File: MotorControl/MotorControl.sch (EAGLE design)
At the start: 6 parts

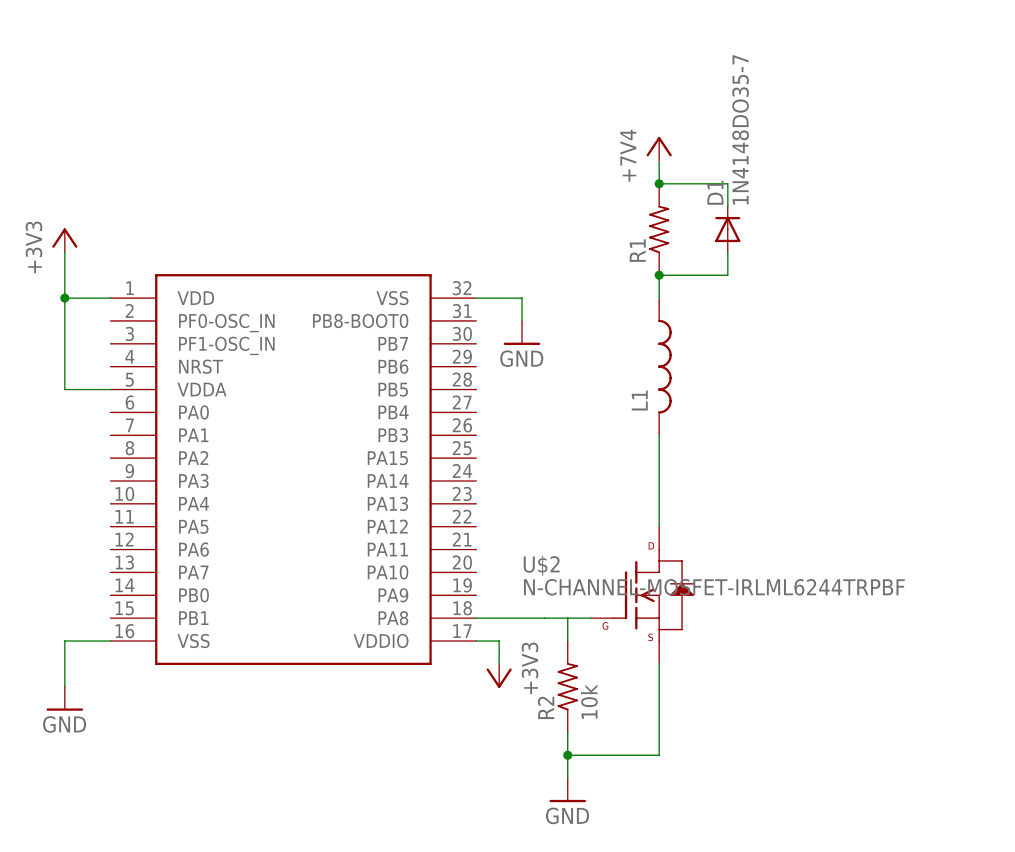
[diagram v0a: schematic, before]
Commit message: Update motor control schematic
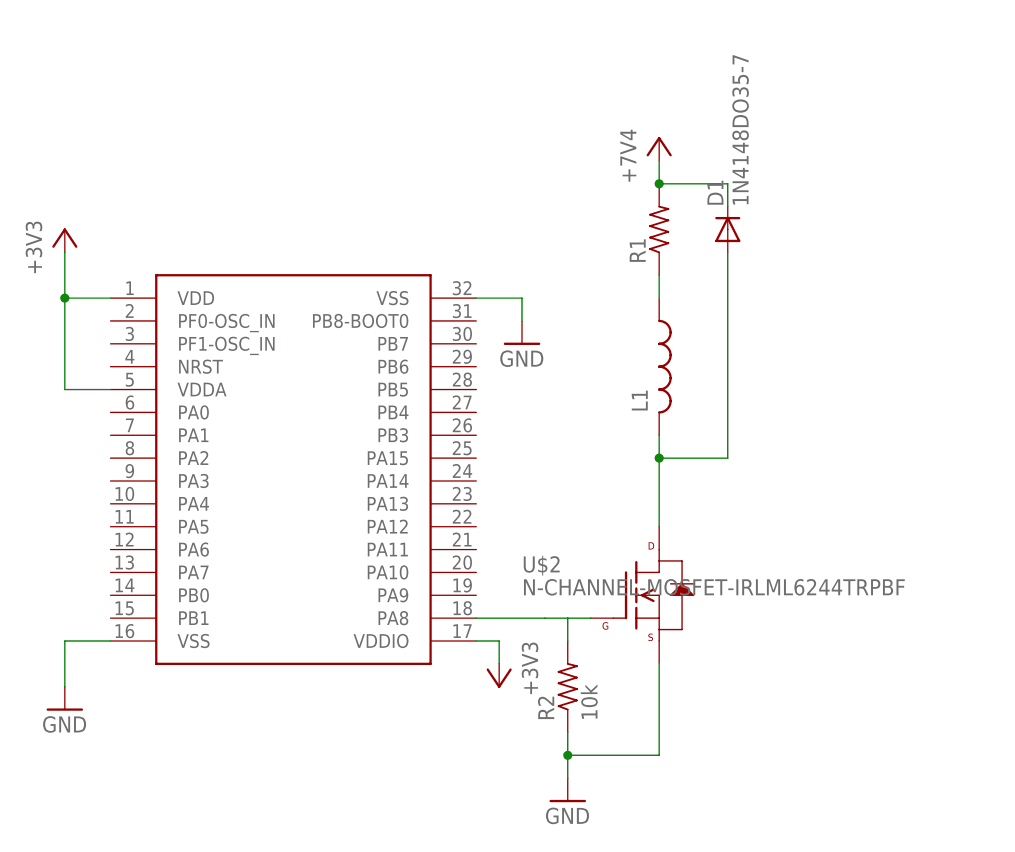
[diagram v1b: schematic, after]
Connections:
- removed net N$4: L1.2, U$2.D
- new net N$2: L1.1, R1.1
- net N$5: now also L1.2, U$2.D; no longer L1.1, R1.1
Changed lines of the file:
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@@
-</segment>
-</net>
-<net name="N$4" class="0">
-<segment>
-<pinref part="U$2" gate="G$1" pin="D"/>
-<pinref part="L1" gate="G$1" pin="2"/>
-<wire x1="40.64" y1="-2.54" x2="40.64" y2="7.62" width="0.1524" layer="91"/>
 </segment>
 </net>
 <net name="N$5" class="0">
 <segment>
-<pinref part="L1" gate="G$1" pin="1"/>
-<pinref part="R1" gate="G$1" pin="1"/>
-<wire x1="40.64" y1="22.86" x2="40.64" y2="25.4" width="0.1524" layer="91"/>
 <pinref part="D1" gate="G$1" pin="A"/>
-<wire x1="40.64" y1="25.4" x2="48.26" y2="25.4" width="0.1524" layer="91"/>
-<wire x1="48.26" y1="25.4" x2="48.26" y2="27.94" width="0.1524" layer="91"/>
-<junction x="40.64" y="25.4"/>
+<pinref part="U$2" gate="G$1" pin="D"/>
+<pinref part="L1" gate="G$1" pin="2"/>
+<wire x1="40.64" y1="-2.54" x2="40.64" y2="5.08" width="0.1524" layer="91"/>
+<wire x1="40.64" y1="5.08" x2="40.64" y2="7.62" width="0.1524" layer="91"/>
+<wire x1="48.26" y1="27.94" x2="48.26" y2="5.08" width="0.1524" layer="91"/>
+<wire x1="48.26" y1="5.08" x2="40.64" y2="5.08" width="0.1524" layer="91"/>
+<junction x="40.64" y="5.08"/>
 </segment>
 </net>
@@
 </segment>
 </net>
+<net name="N$2" class="0">
+<segment>
+<pinref part="R1" gate="G$1" pin="1"/>
+<pinref part="L1" gate="G$1" pin="1"/>
+<wire x1="40.64" y1="22.86" x2="40.64" y2="25.4" width="0.1524" layer="91"/>
+</segment>
+</net>
